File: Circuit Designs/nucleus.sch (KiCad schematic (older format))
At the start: 88 parts

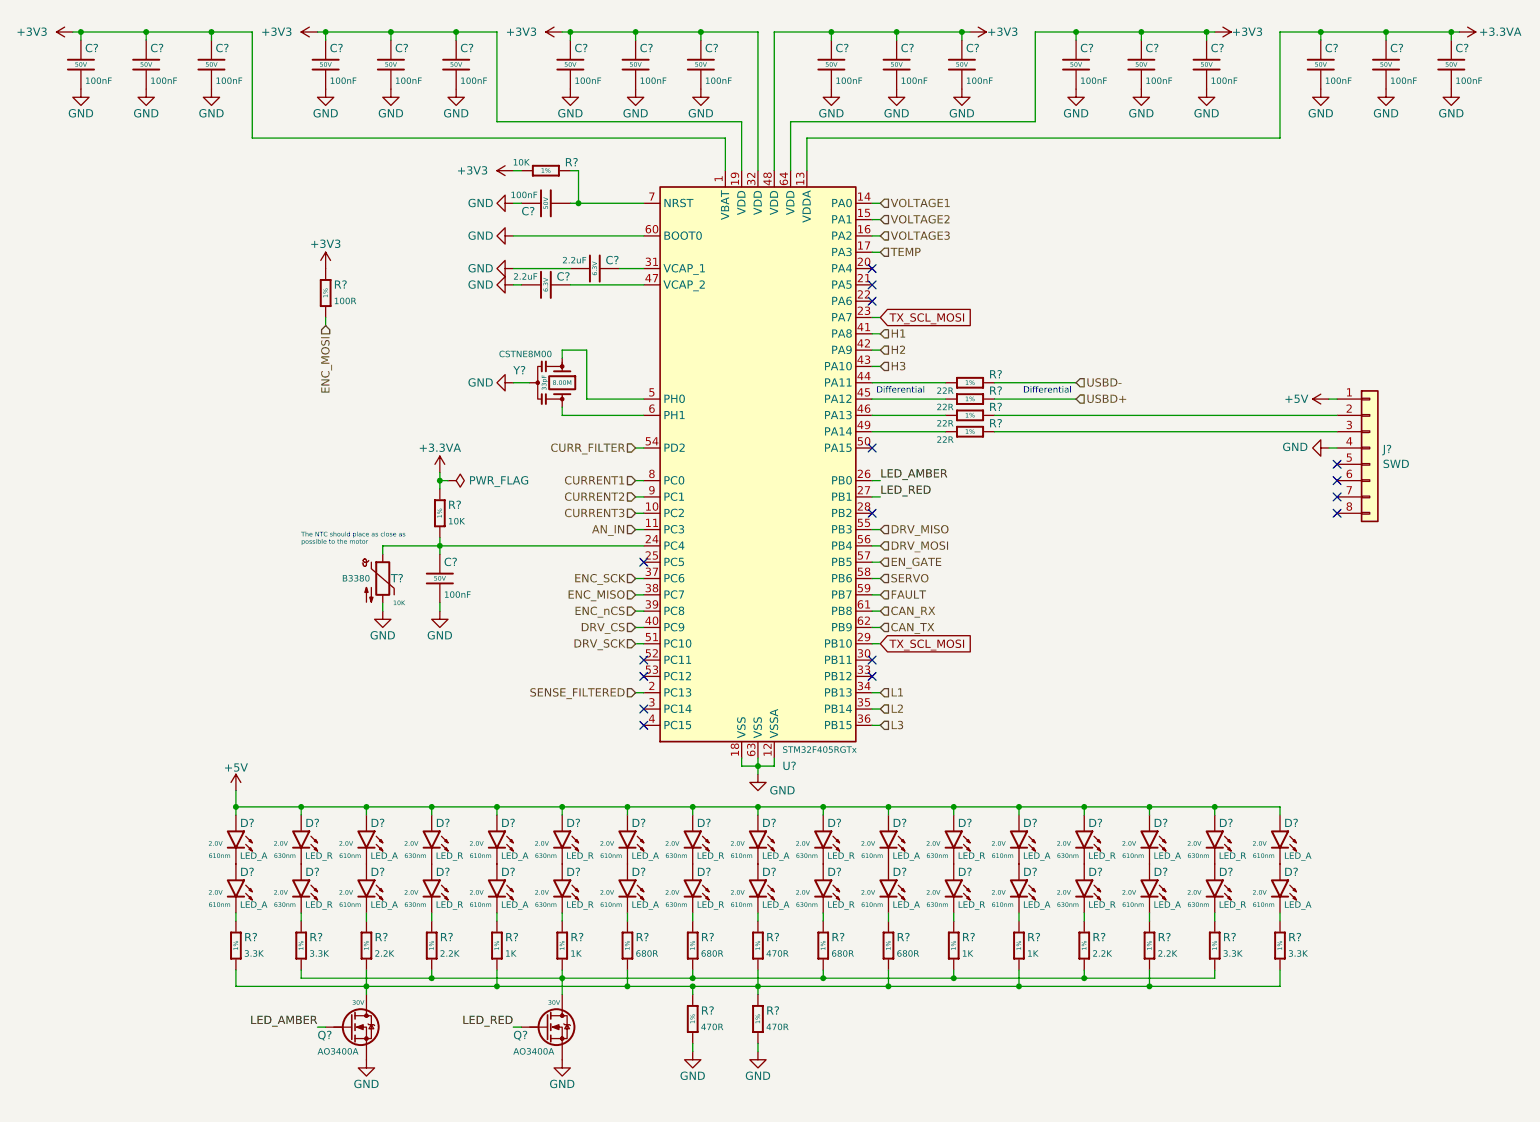
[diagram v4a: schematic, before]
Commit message: edited myofibril file, added a related image about myofibrils
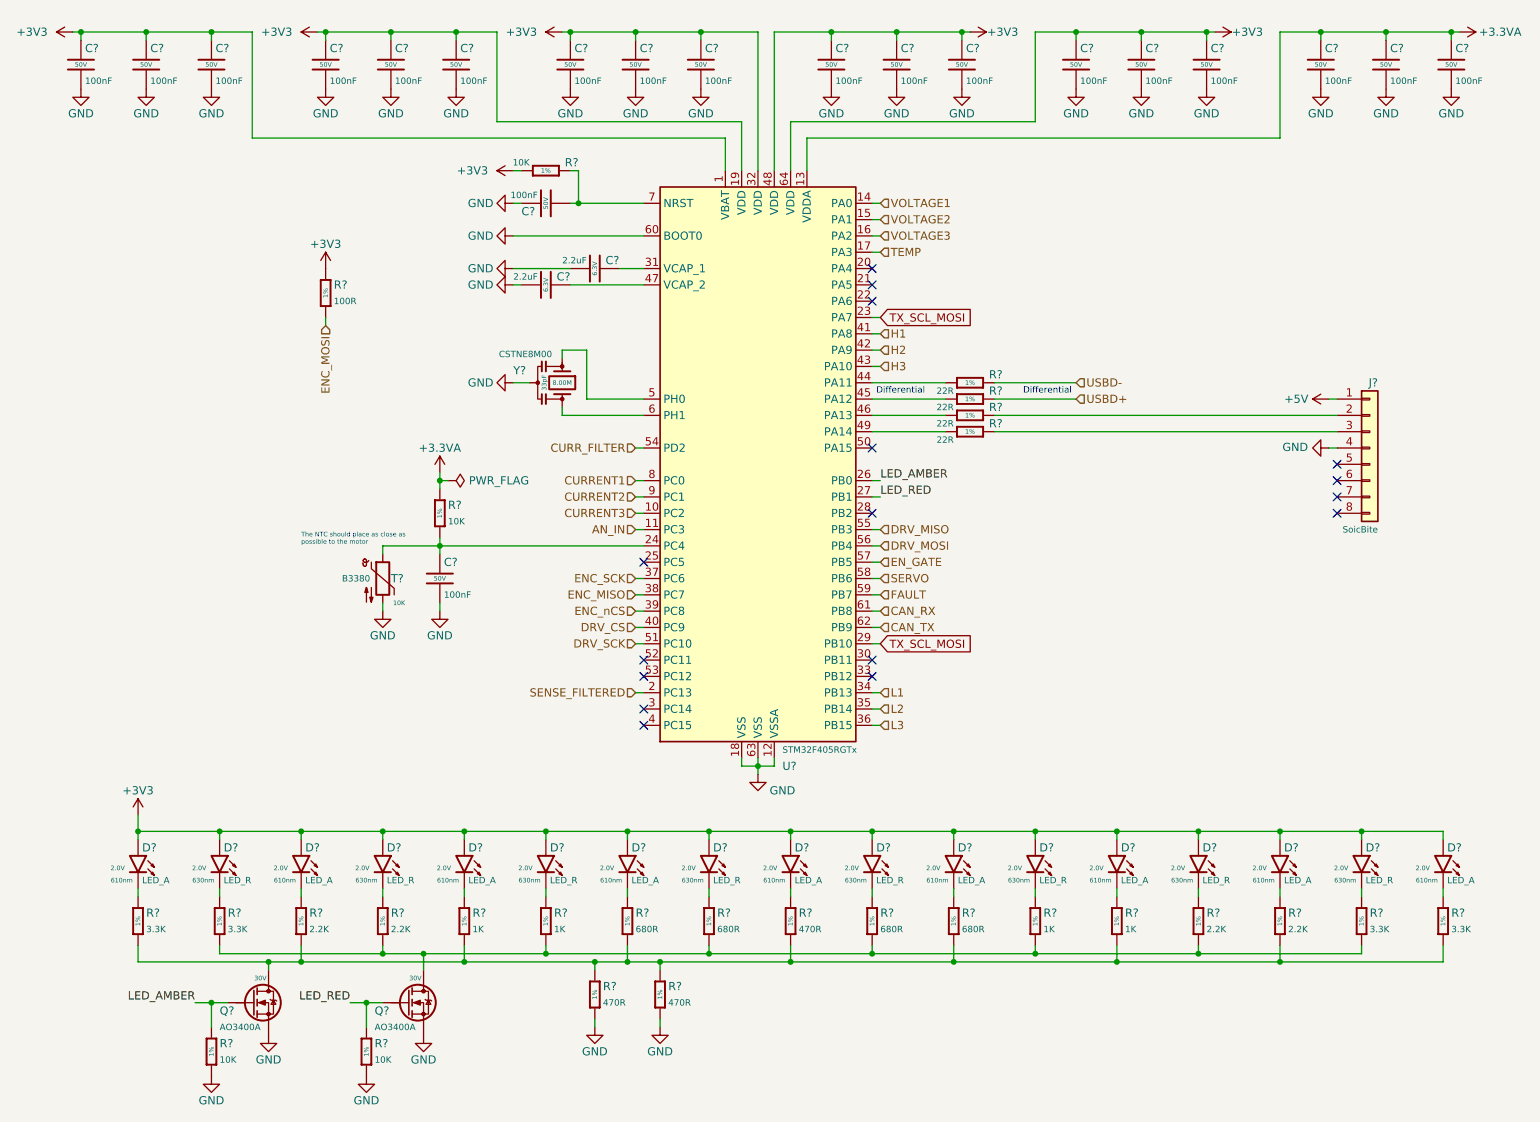
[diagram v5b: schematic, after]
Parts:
- removed D? (x9): LED_A, LED_SMD:LED_0603_1608Metric, symbol CoE_Diode:LED_A
- removed D? (x8): LED_R, LED_SMD:LED_0603_1608Metric, symbol CoE_Diode:LED_R
- removed J?: SWD, symbol Connector_Generic:Conn_01x08
- added J?: SoicBite, symbol CoE_Connector:SoicBite
- added R? (x2): 10K, Resistor_SMD:R_0402_1005Metric, symbol CoE_Resistor:10K
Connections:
- net +3V3: now also D?.2 (A), D?.2 (A), D?.2 (A), D?.2 (A), D?.2 (A), D?.2 (A), D?.2 (A), D?.2 (A), D?.2 (A), D?.2 (A), D?.2 (A), D?.2 (A), D?.2 (A), D?.2 (A), D?.2 (A), D?.2 (A), D?.2 (A)
- net +5V: now also J?.1 (Pin_1)
- net GND: now also J?.4 (Pin_4), R?.2, R?.2
- net LED_AMBER: now also R?.1
- net LED_RED: now also R?.1
- net at R?.2: now also J?.2 (Pin_2)
- net at R?.2: now also J?.3 (Pin_3)
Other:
- moved on the sheet: D?, Q?, R?
